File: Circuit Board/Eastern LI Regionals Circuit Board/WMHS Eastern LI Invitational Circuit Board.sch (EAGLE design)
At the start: 361 parts, among them IC1101 7805DT, IC1201 7805DT, IC1301 7805DT, IC1501 7805DT, J1005 ICSP_HEADER, J1104 ICSP_HEADER, J1204 ICSP_HEADER, J1304 ICSP_HEADER, J204 ICSP_HEADER, J301 ICSP_HEADER, J401 ICSP_HEADER, J503 ICSP_HEADER, J603 ICSP_HEADER, J703 ICSP_HEADER, J704 ICSP_HEADER, J903 ICSP_HEADER, Q1001 PSMN7R0-60YS, Q1401 PSMN7R0-60YS, Q201 PSMN7R0-60YS, Q301 500mA/300V, Q401 500mA/300V, Q501 PSMN7R0-60YS, Q601 PSMN7R0-60YS, Q801 PSMN7R0-60YS, Q901 PSMN7R0-60YS, U1001 ATTINY25-20SSUR, U1002 MIC5205, U101 74HC1G04, U102 MIC5205, U1101 DRV8835, U1102 ATTINY25-20SSUR, U1201 DRV8835, U1202 ATTINY25-20SSUR, U1301 DRV8835, U1302 ATTINY25-20SSUR, U1401 74HC1G04, U1402 MIC5205, U201 74HC1G04, U202 ATTINY25-20SSUR, U203 MIC5205, U301 74HC1G04, U302 SN74C1G08-DCK, U303 ATTINY25-20SSUR, U304 MIC5205, U401 74HC1G04, U402 SN74C1G08-DCK, U403 ATTINY25-20SSUR, U404 MIC5205, U501 74HC1G04, U502 SN74C1G08-DCK, U503 ATTINY25-20SSUR, U504 MIC5205, U601 74HC1G04, U602 SN74C1G08-DCK, U603 ATTINY25-20SSUR, U604 MIC5205, U701 ATTINY25-20SSUR, U702 ATTINY25-20SSUR, U703 MIC5205, U801 74HC1G04, U802 SN74C1G08-DCK, U803 MIC5205, U901 ATTINY25-20SSUR, U902 MIC5205, X1601 MSTBA2

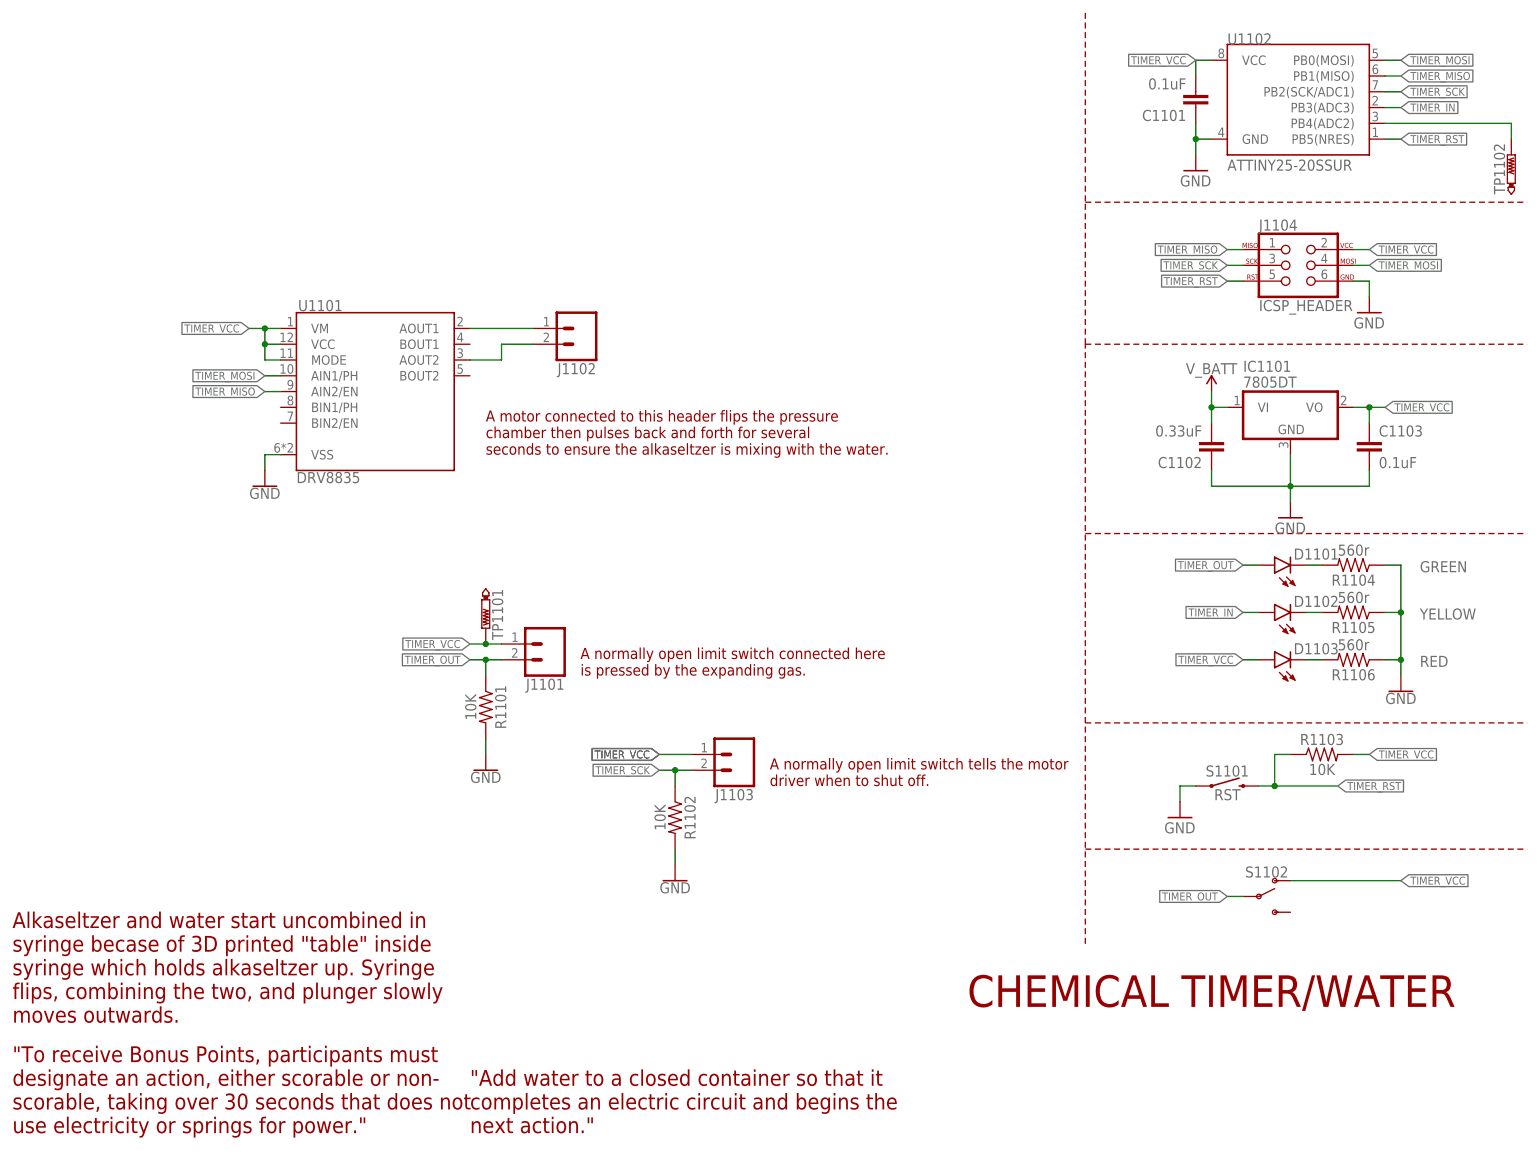
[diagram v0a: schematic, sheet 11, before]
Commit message: Changed file naming system
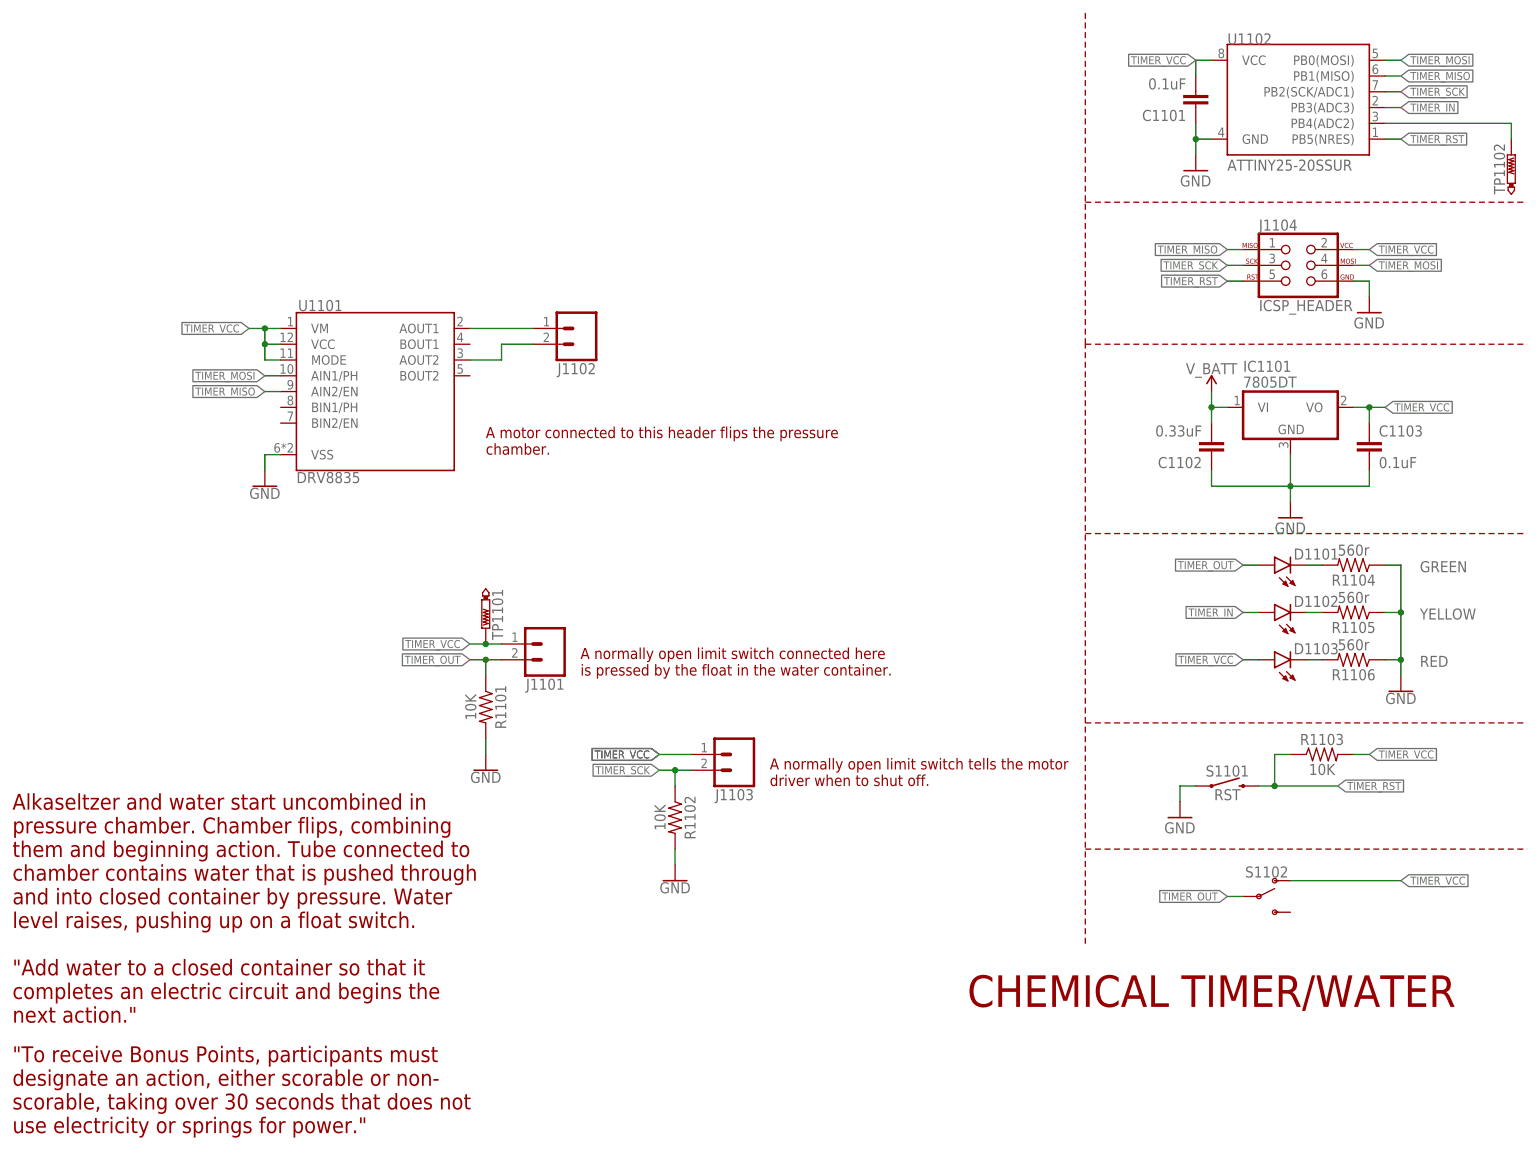
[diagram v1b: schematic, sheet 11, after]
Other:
- note added: "A motor connected to this header flips the pressure chamber."
- note added: "A normally open limit switch connected here is pressed by the float in the water container."
- note added: "Alkaseltzer and water start uncombined in pressure chamber. Chamber flips, combining them and beginning action. Tube connected to chamber contains water that is pushed through and into closed container by pressure. Water level raises, pushing up on a float switch."
- note added: "Pressure chamber with baking soda and 30% warm vinegar is flipped, the two react and the resulting reaction inflates a balloon which hits a limit switch 20cm away."
- note removed: "A motor connected to this header flips the pressure chamber then pulses back and forth for several seconds to ensure the alkaseltzer is mixing with the water."
- note removed: "A normally open limit switch connected here is pressed by the expanding gas."
- note removed: "Alkaseltzer and water start uncombined in syringe becase of 3D printed "table" inside syringe which holds alkaseltzer up. Syringe flips, combining the two, and plunger slowly moves outwards."
- note removed: "Syringe with baking soda filled basket attached to plunger is filled with 30% warm vinegar. When syringe is flipped, the two react and the resulting reaction inflates a balloon which hits a limit switch 20cm away."
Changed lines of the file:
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@@
 use electricity or springs for power."</text>
 <text x="96.52" y="78.74" size="1.778" layer="94">A normally open limit switch connected here
-is pressed by the expanding gas.</text>
+is pressed by the float in the water container.</text>
 <text x="81.28" y="114.3" size="1.778" layer="94">A motor connected to this header flips the pressure
-chamber then pulses back and forth for several
-seconds to ensure the alkaseltzer is mixing with the water.</text>
+chamber.</text>
 <wire x1="177.8" y1="185.42" x2="177.8" y2="154.94" width="0.1524" layer="94" style="dashdot"/>
 <wire x1="177.8" y1="154.94" x2="248.92" y2="154.94" width="0.1524" layer="94" style="longdash"/>
@@
 <text x="127" y="60.96" size="1.778" layer="94">A normally open limit switch tells the motor
 driver when to shut off.</text>
-<text x="5.08" y="22.86" size="2.54" layer="94">Alkaseltzer and water start uncombined in
-syringe becase of 3D printed "table" inside
-syringe which holds alkaseltzer up. Syringe
-flips, combining the two, and plunger slowly
-moves outwards.</text>
-<text x="78.74" y="5.08" size="2.54" layer="94">"Add water to a closed container so that it
+<text x="5.08" y="38.1" size="2.54" layer="94">Alkaseltzer and water start uncombined in
+pressure chamber. Chamber flips, combining
+them and beginning action. Tube connected to
+chamber contains water that is pushed through
+and into closed container by pressure. Water
+level raises, pushing up on a float switch.</text>
+<text x="5.08" y="22.86" size="2.54" layer="94">"Add water to a closed container so that it
 completes an electric circuit and begins the
 next action."</text>
@@
 <text x="109.22" y="66.04" size="1.778" layer="94">A normally open limit switch tells the motor
 driver when to shut off.</text>
-<text x="5.08" y="25.4" size="2.54" layer="94">Syringe with baking soda filled basket attached
-to plunger is filled with 30% warm vinegar.
-When syringe is flipped, the two react and the
+<text x="5.08" y="25.4" size="2.54" layer="94">Pressure chamber with baking soda and 30%
+warm vinegar is flipped, the two react and the
 resulting reaction inflates a balloon which hits
 a limit switch 20cm away.</text>

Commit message: SOUP and States Upgrades and Modifications
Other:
- note added: "Jumpers are installed on all of the above headers, with the following exceptions: J1605 ENDO_OUT -> J1606 IR_IN J1606 WATER_OUT -> J1611 BALLOON_IN"
- note added: "Update 1/26/2018: Action has been combined with timer action. The mosfet is no longer required, but the microcontroller is being used as a switch with the water level and two probes."
- note removed: "Update 1/22/2018: Action has been combined with timer action. New action is better suited to the electronics available on the timer section, so none of these components are being used and the transfer will be bypassed via jumpers."
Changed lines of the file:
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@@
 <wire x1="12.7" y1="154.94" x2="12.7" y2="63.5" width="0.1524" layer="98" style="shortdash"/>
 <wire x1="246.38" y1="38.1" x2="246.38" y2="180.34" width="0.1524" layer="98" style="shortdash"/>
-<text x="15.24" y="160.02" size="1.778" layer="98">Update 1/22/2018: Action has been combined
-with timer action. New action is better suited to
-the electronics available on the timer section,
-so none of these components are being used
-and the transfer will be bypassed via jumpers.</text>
+<text x="15.24" y="160.02" size="1.778" layer="98">Update 1/26/2018: Action has been combined
+with timer action. The mosfet is no longer
+required, but the microcontroller is being used
+as a switch with the water level and two
+probes.</text>
 <wire x1="12.7" y1="63.5" x2="175.26" y2="63.5" width="0.1524" layer="98" style="shortdash"/>
 <wire x1="175.26" y1="63.5" x2="175.26" y2="38.1" width="0.1524" layer="98" style="shortdash"/>
@@
 <plain>
 <text x="198.12" y="27.94" size="4.826" layer="94" align="center">Power and Inter-Action</text>
+<text x="50.8" y="27.94" size="1.778" layer="98">Jumpers are installed on all of the above
+headers, with the following exceptions:
+J1605 ENDO_OUT -&gt; J1606 IR_IN
+J1606 WATER_OUT -&gt; J1611 BALLOON_IN  </text>
 </plain>
 <instances>
